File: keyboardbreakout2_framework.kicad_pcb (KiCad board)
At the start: 2 copper layers, 21.5 x 12.5 mm, 4 parts, among them U1 10156001-051100LF

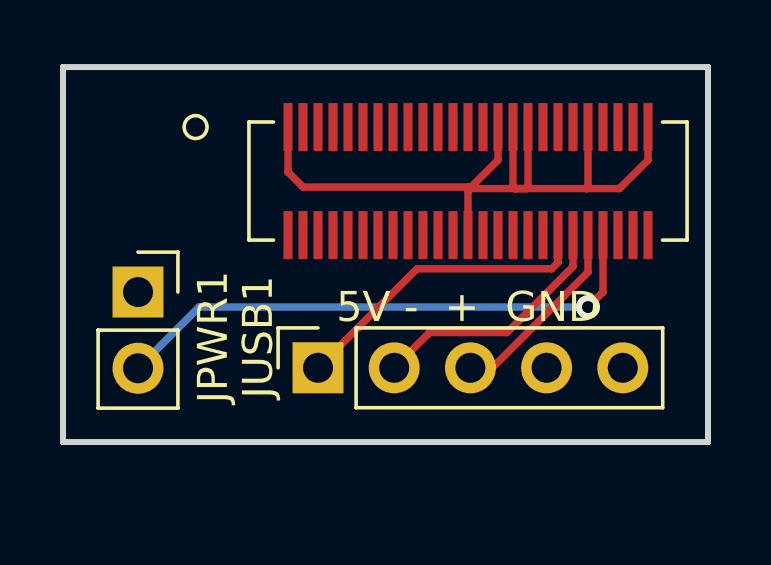
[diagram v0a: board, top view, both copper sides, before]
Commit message: added second row to usb-headers because most adapters on amazon have two rows (only one connector works tho)
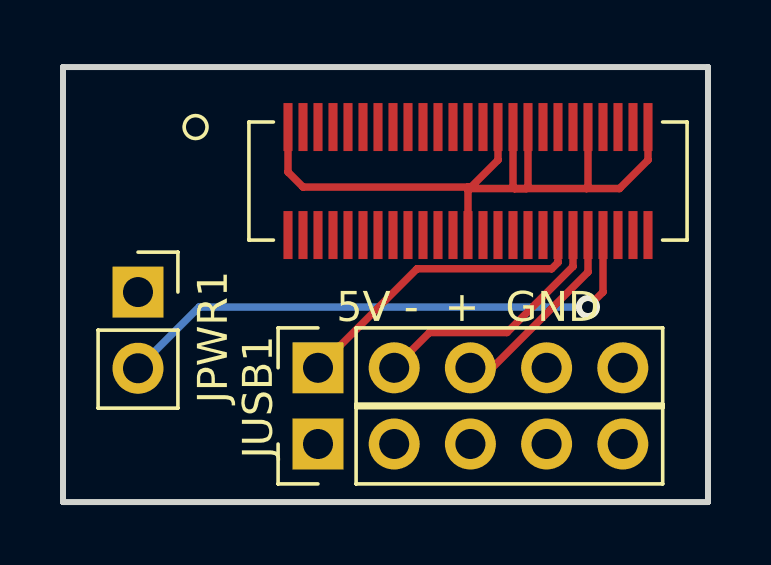
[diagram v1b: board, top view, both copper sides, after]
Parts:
- added REF**: PinHeader_1x05_P2.54mm_Vertical, Connector_PinHeader_2.54mm:PinHeader_1x05_P2.54mm_Vertical, F.Cu at (81.5, 57.1)
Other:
- board size 21.5 x 12.5 mm -> 21.5 x 14.5 mm
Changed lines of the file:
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@@
   (net 43 "unconnected-(U1-Pad50)")
   (net 44 "GND")
+  (footprint "Connector_PinHeader_2.54mm:PinHeader_1x05_P2.54mm_Vertical" (layer "F.Cu")
+    (at 81.5 57.065 90)
+    (descr "Through hole straight pin header, 1x05, 2.54mm pitch, single row")
+    (tags "Through hole pin header THT 1x05 2.54mm single row")
+    (attr through_hole)
+    (fp_text reference "REF**" (at 0 -2.33 90) (layer "F.SilkS") hide
+      (effects (font (size 1 1) (thickness 0.15)))
+    )
+    (fp_text value "PinHeader_1x05_P2.54mm_Vertical" (at 0 12.49 90) (layer "F.Fab") hide
+      (effects (font (size 1 1) (thickness 0.15)))
+    )
+    (fp_text user "${REFERENCE}" (at 0 5.08) (layer "F.Fab") hide
+      (effects (font (size 1 1) (thickness 0.15)))
+    )
+    (fp_line (start -1.33 0) (end -1.33 -1.33) (layer "F.SilkS") (width 0.12))
+    (fp_line (start -1.33 -1.33) (end 0 -1.33) (layer "F.SilkS") (width 0.12))
+    (fp_line (start -1.33 1.27) (end 1.33 1.27) (layer "F.SilkS") (width 0.12))
+    (fp_line (start -1.33 11.49) (end 1.33 11.49) (layer "F.SilkS") (width 0.12))
+    (fp_line (start 1.33 1.27) (end 1.33 11.49) (layer "F.SilkS") (width 0.12))
+    (fp_line (start -1.33 1.27) (end -1.33 11.49) (layer "F.SilkS") (width 0.12))
+    (fp_line (start -1.8 -1.8) (end -1.8 11.95) (layer "F.CrtYd") (width 0.05))
+    (fp_line (start -1.8 11.95) (end 1.8 11.95) (layer "F.CrtYd") (width 0.05))
+    (fp_line (start 1.8 11.95) (end 1.8 -1.8) (layer "F.CrtYd") (width 0.05))
+    (fp_line (start 1.8 -1.8) (end -1.8 -1.8) (layer "F.CrtYd") (width 0.05))
+    (fp_line (start -0.635 -1.27) (end 1.27 -1.27) (layer "F.Fab") (width 0.1))
+    (fp_line (start -1.27 11.43) (end -1.27 -0.635) (layer "F.Fab") (width 0.1))
+    (fp_line (start 1.27 -1.27) (end 1.27 11.43) (layer "F.Fab") (width 0.1))
+    (fp_line (start -1.27 -0.635) (end -0.635 -1.27) (layer "F.Fab") (width 0.1))
+    (fp_line (start 1.27 11.43) (end -1.27 11.43) (layer "F.Fab") (width 0.1))
+    (pad "1" thru_hole rect (at 0 0 90) (size 1.7 1.7) (drill 1) (layers *.Cu *.Mask))
+    (pad "2" thru_hole oval (at 0 2.54 90) (size 1.7 1.7) (drill 1) (layers *.Cu *.Mask))
+    (pad "3" thru_hole oval (at 0 5.08 90) (size 1.7 1.7) (drill 1) (layers *.Cu *.Mask))
+    (pad "4" thru_hole oval (at 0 7.62 90) (size 1.7 1.7) (drill 1) (layers *.Cu *.Mask))
+    (pad "5" thru_hole oval (at 0 10.16 90) (size 1.7 1.7) (drill 1) (layers *.Cu *.Mask))
+    (model "${KICAD6_3DMODEL_DIR}/Connector_PinHeader_2.54mm.3dshapes/PinHeader_1x05_P2.54mm_Vertical.wrl"
+      (offset (xyz 0 0 0))
+      (scale (xyz 1 1 1))
+      (rotate (xyz 0 0 0))
+    )
+  )
   (footprint "Connector_PinSocket_2.54mm:PinSocket_1x02_P2.54mm_Vertical" (layer "F.Cu")
     (at 75.5 52)
@@
     (property "Sheetname" "")
     (attr through_hole exclude_from_bom)
-    (fp_text reference "JUSB1" (at 1.025 -2 90) (layer "F.SilkS")
+    (fp_text reference "JUSB1" (at -0.975 -2 90) (layer "F.SilkS")
       (effects (font (size 1 1) (thickness 0.15)))
     )
@@
       ) (layer "B.SilkS") (width 0) (fill solid))
   )
-  (gr_rect (start 94.5 57) (end 73 44.5) (layer "Edge.Cuts") (width 0.2) (fill none))
+  (gr_rect (start 94.5 59) (end 73 44.5) (layer "Edge.Cuts") (width 0.2) (fill none))
   (gr_text "5V -  +  GND" (at 86.5 52.5) (layer "F.SilkS")
     (effects (font (size 1 1) (thickness 0.25)))
@@
     (polygon
       (pts
-        (xy 94.5 57)
-        (xy 73 57)
+        (xy 94.5 59)
+        (xy 73 59)
         (xy 73 44.5)
         (xy 94.5 44.5)

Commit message: added connector for power-button LEDs
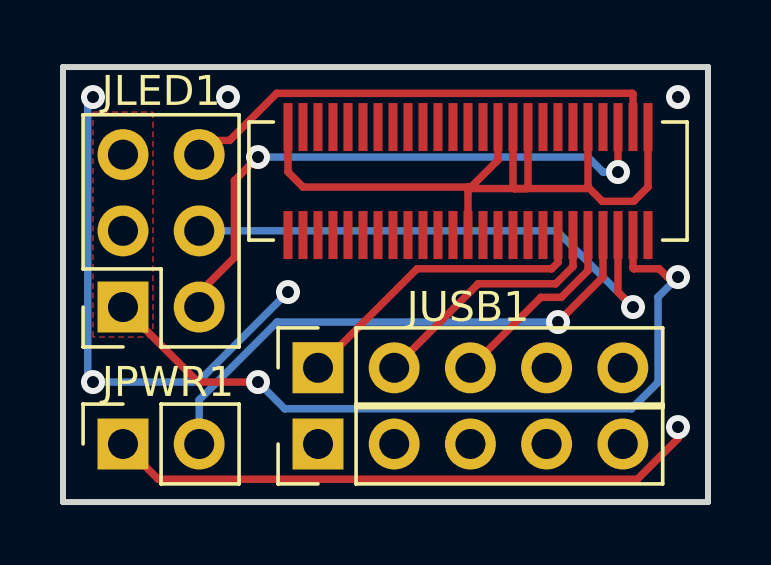
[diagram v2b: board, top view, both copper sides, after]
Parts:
- added JLED1: Conn_02x03_Odd_Even, Connector_PinSocket_2.54mm:PinSocket_2x03_P2.54mm_Vertical, F.Cu at (75.0, 52.5)
- moved JPWR1 5.09 mm to (75.0, 57.1), turned to 90 degrees
- moved G*** 3.50 mm to (89.0, 49.0), turned to 0 degrees
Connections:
- U1 pad 23: unconnected-(U1-Pad23) -> Net-(U1-Pad23)
- U1 pad 24: unconnected-(U1-Pad24) -> Net-(U1-Pad24)
- U1 pad 27: unconnected-(U1-Pad27) -> +5V
- U1 pad 28: unconnected-(U1-Pad28) -> Net-(U1-Pad28)
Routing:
- net GND: track 25.9 -> 64.0 mm, vias 0 -> 6
- net +5V: track 0.00 -> 26.1 mm, vias 0 -> 2
- net Net-(U1-Pad23): track 0.00 -> 19.0 mm, vias 0 -> 2
- net Net-(U1-Pad28): track 0.00 -> 18.1 mm, vias 0 -> 1
- net Net-(U1-Pad24): track 0.00 -> 16.2 mm
- added copper zone on F.Cu, net +5V
- added copper zone on B.Cu, net GND
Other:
- board text added: "5V D- D+ GND NC"
- board text added: "5V LED"
- board text added: "Designed by Dekkia CC BY-NC-SA 4.0"
- board text added: "GND PWR"
- board text added: "R W G"
- board text added: "RAM"
- board text removed: "5V - + GND"
